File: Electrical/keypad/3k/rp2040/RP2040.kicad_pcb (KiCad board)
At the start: 4 copper layers, 67.7 x 67.4 mm, 79 parts, among them J1 Conn_01x04_Socket, P1 USB-TYPE-C-016, Q1 BSS138, SW1 TS-1187A-B-A-B, SW2 TS-1187A-B-A-B, SW3 BUTT1, SW4 BUTT3, SW5 BUTT2, U1 PRTR5V0U2X, U2 ME6208A44M3G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

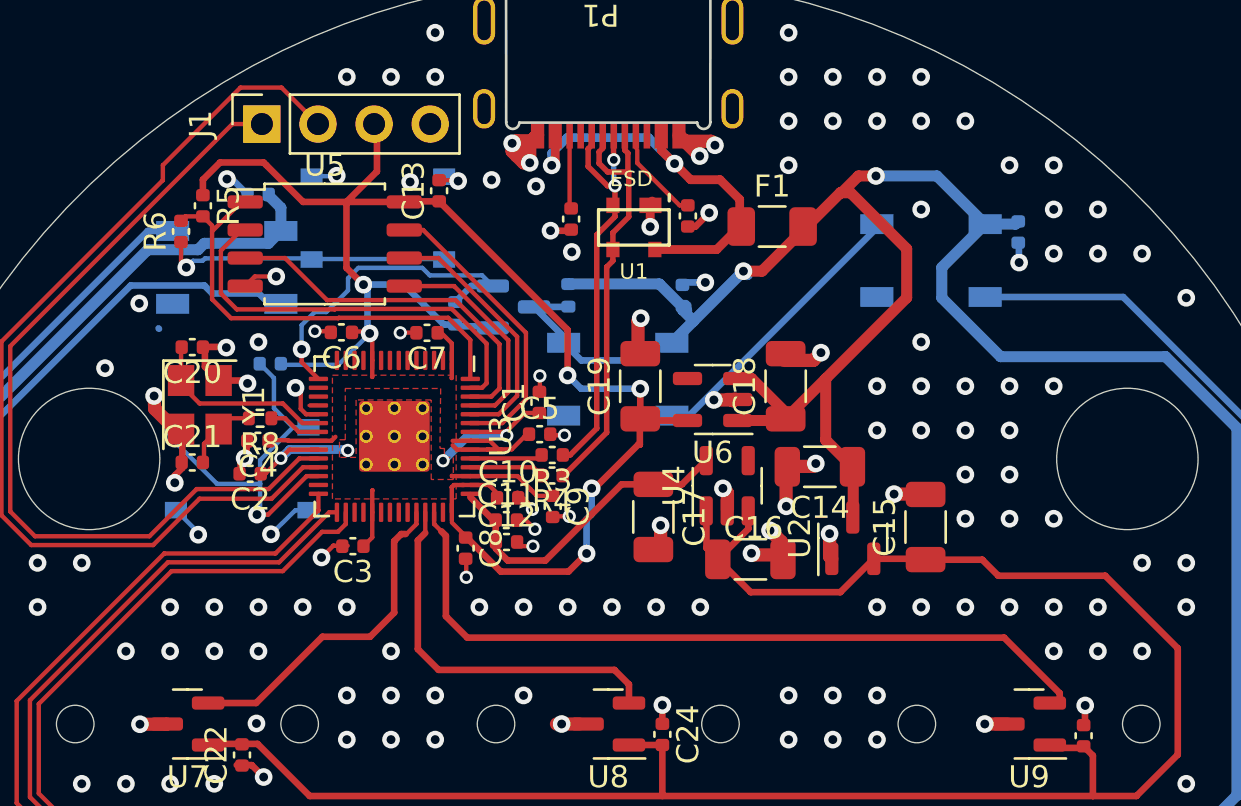
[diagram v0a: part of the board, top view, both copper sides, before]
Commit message: improves component placement
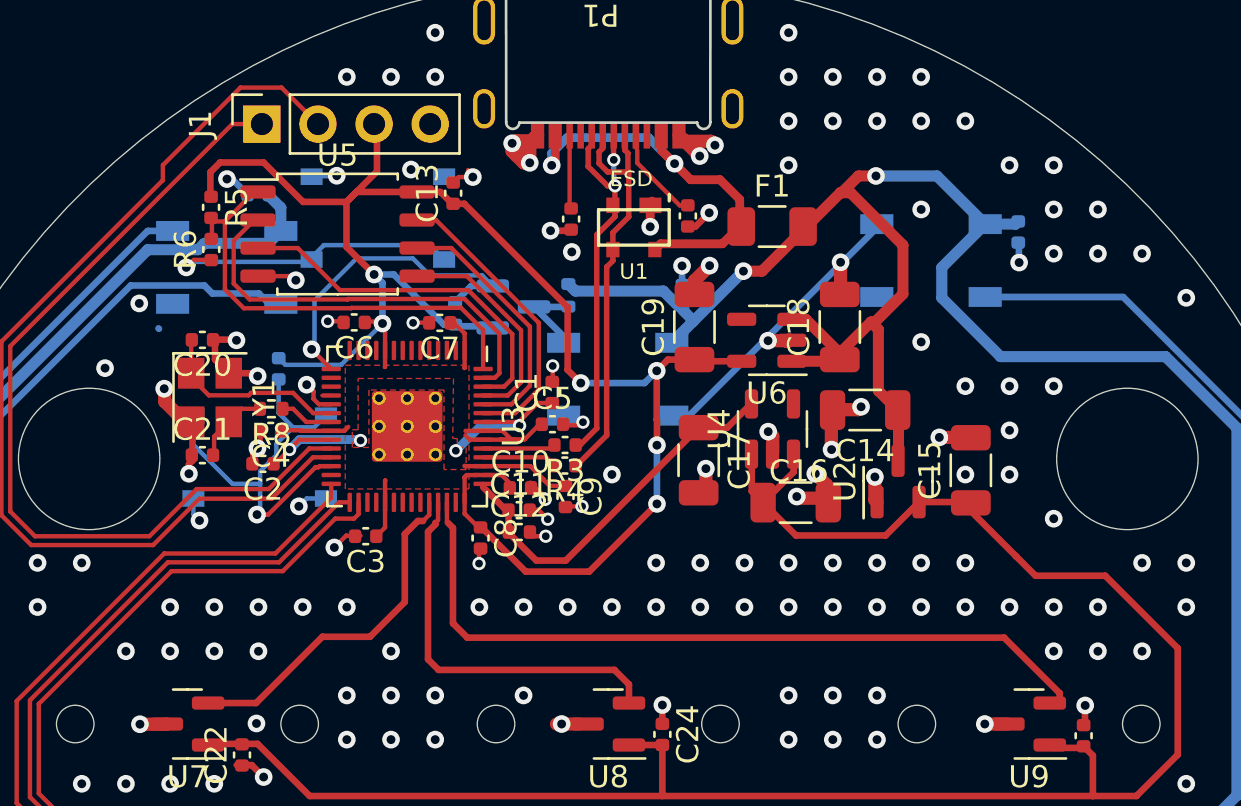
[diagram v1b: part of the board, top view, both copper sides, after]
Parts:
- moved U6 3.63 mm to (107.2, 82.6)
- moved C18 3.63 mm to (110.5, 82.0)
- moved C19 3.63 mm to (103.9, 82.0)
- moved C14 3.29 mm to (111.6, 85.8)
- moved U4 3.29 mm to (107.4, 86.6)
- moved C15 3.29 mm to (116.4, 88.5)
- moved C17 3.29 mm to (104.1, 88.1)
- moved U2 3.29 mm to (113.1, 89.0)
- moved C16 3.29 mm to (108.5, 90.0)
- moved R6 1.60 mm to (82.0, 78.5)
- moved SW2 0.95 mm to (84.2, 87.9)
- moved C8 0.82 mm to (94.2, 91.6)
- moved C10 0.73 mm to (96.0, 89.3)
- moved C12 0.73 mm to (96.0, 91.3)
- moved C3 0.73 mm to (89.0, 91.5)
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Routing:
- net +5V: track 273.7 -> 269.2 mm
- net Net-(D4-DIN): track 6.76 -> 3.41 mm
- net +3V3: track 88.1 -> 91.3 mm
- net ADC_AVDD: track 14.8 -> 17.4 mm
- net GND: track 93.8 -> 91.5 mm, vias 313 -> 315
- net +4V4: track 87.6 -> 86.7 mm
- net BUTT2: track 71.1 -> 71.9 mm
- net USB_D+: track 19.1 -> 18.4 mm
- net SWDIO: track 44.4 -> 45.2 mm
- net BUTT1: track 59.2 -> 59.9 mm
- net SWCLK: track 38.9 -> 39.7 mm
- net USB_D-: track 20.0 -> 19.3 mm
- net ADC_IN1: track 15.2 -> 15.8 mm
- net BUTT0: track 48.7 -> 49.4 mm
- net /QSPI_SS: track 21.3 -> 20.7 mm
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
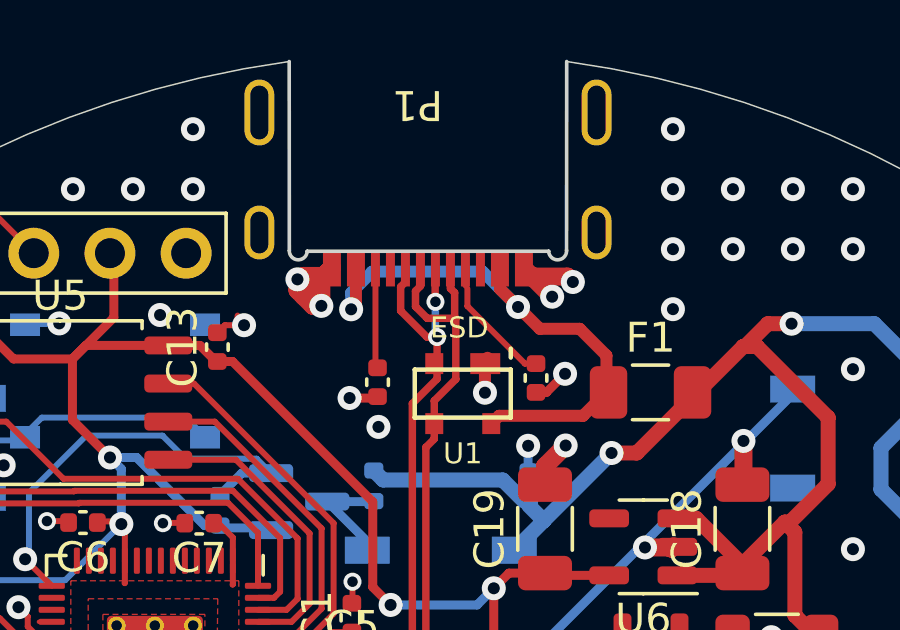
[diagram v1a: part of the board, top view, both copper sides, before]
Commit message: adds gnd vias near connector
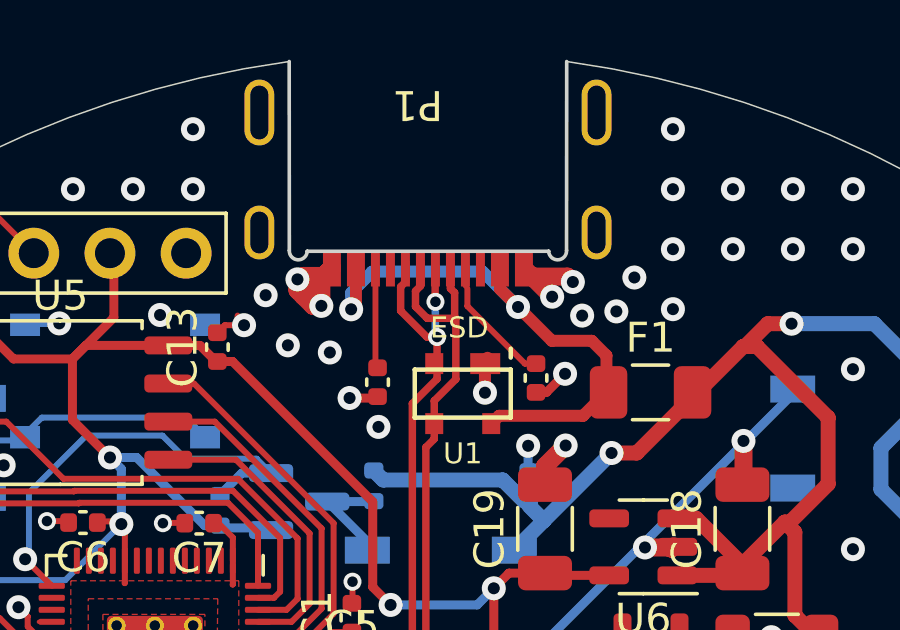
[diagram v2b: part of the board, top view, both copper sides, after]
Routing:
- net GND: vias 315 -> 321
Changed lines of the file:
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@@
   (via (at 104.166 130.706) (size 0.8) (drill 0.4) (layers "F.Cu" "B.Cu") (free) (net 1))
   (via (at 114.166 70.706) (size 0.8) (drill 0.4) (layers "F.Cu" "B.Cu") (free) (net 1))
+  (via (at 105.14 74.92) (size 0.8) (drill 0.4) (layers "F.Cu" "B.Cu") (free) (net 1))
   (via (at 112.166 128.706) (size 0.8) (drill 0.4) (layers "F.Cu" "B.Cu") (free) (net 1))
   (via (at 110.166 70.706) (size 0.8) (drill 0.4) (layers "F.Cu" "B.Cu") (free) (net 1))
@@
   (via (at 111.76 123.19) (size 0.8) (drill 0.4) (layers "F.Cu" "B.Cu") (free) (net 1))
   (via (at 100.166 88.706) (size 0.8) (drill 0.4) (layers "F.Cu" "B.Cu") (free) (net 1))
+  (via (at 94.59 74.24) (size 0.8) (drill 0.4) (layers "F.Cu" "B.Cu") (free) (net 1))
   (via (at 112.166 108.706) (size 0.8) (drill 0.4) (layers "F.Cu" "B.Cu") (free) (net 1))
   (via (at 93.135 123.165) (size 0.8) (drill 0.4) (layers "F.Cu" "B.Cu") (net 1))
@@
   (via (at 88.166 70.706) (size 0.8) (drill 0.4) (layers "F.Cu" "B.Cu") (free) (net 1))
   (via (at 114.166 128.706) (size 0.8) (drill 0.4) (layers "F.Cu" "B.Cu") (free) (net 1))
+  (via (at 95.33 75.91) (size 0.8) (drill 0.4) (layers "F.Cu" "B.Cu") (free) (net 1))
   (via (at 98.815162 90.1495) (size 0.6) (drill 0.35) (layers "F.Cu" "B.Cu") (net 1))
   (via (at 88.166 106.706) (size 0.8) (drill 0.4) (layers "F.Cu" "B.Cu") (free) (net 1))
@@
   (via (at 92.166 112.706) (size 0.8) (drill 0.4) (layers "F.Cu" "B.Cu") (free) (net 1))
   (via (at 108.166 130.706) (size 0.8) (drill 0.4) (layers "F.Cu" "B.Cu") (free) (net 1))
+  (via (at 106.28 74.78) (size 0.8) (drill 0.4) (layers "F.Cu" "B.Cu") (free) (net 1))
   (via (at 86.166 112.706) (size 0.8) (drill 0.4) (layers "F.Cu" "B.Cu") (free) (net 1))
   (via (at 130.166 98.706) (size 0.8) (drill 0.4) (layers "F.Cu" "B.Cu") (free) (net 1))
@@
   (via (at 108.166 112.706) (size 0.8) (drill 0.4) (layers "F.Cu" "B.Cu") (free) (net 1))
   (via (at 114.166 106.706) (size 0.8) (drill 0.4) (layers "F.Cu" "B.Cu") (free) (net 1))
+  (via (at 96.73 76.15) (size 0.8) (drill 0.4) (layers "F.Cu" "B.Cu") (free) (net 1))
   (via (at 96.166 94.706) (size 0.8) (drill 0.4) (layers "F.Cu" "B.Cu") (free) (net 1))
   (via (at 84.075 99.975) (size 0.8) (drill 0.4) (layers "F.Cu" "B.Cu") (free) (net 1))
@@
   (via (at 88.166 108.706) (size 0.8) (drill 0.4) (layers "F.Cu" "B.Cu") (free) (net 1))
   (via (at 74.166 94.706) (size 0.8) (drill 0.4) (layers "F.Cu" "B.Cu") (free) (net 1))
+  (via (at 106.88 73.65) (size 0.8) (drill 0.4) (layers "F.Cu" "B.Cu") (free) (net 1))
   (via (at 98.166 94.706) (size 0.8) (drill 0.4) (layers "F.Cu" "B.Cu") (free) (net 1))
   (via (at 108.166 124.706) (size 0.8) (drill 0.4) (layers "F.Cu" "B.Cu") (free) (net 1))
@@
   (segment (start 77.2 108.65) (end 77.01 108.67) (width 0.2) (layer "B.Cu") (net 1))
   (segment (start 104.045 107.145) (end 104.045 107.195) (width 0.3) (layer "B.Cu") (net 1))
-  (segment (start 105.06 75.36) (end 105.95 76.25) (width 0.4) (layer "F.Cu") (net 2))
   (segment (start 105.95 77.48) (end 105.17 78.26) (width 0.4) (layer "F.Cu") (net 2))
+  (segment (start 104.129891 75.76) (end 105.46 75.76) (width 0.4) (layer "F.Cu") (net 2))
+  (segment (start 105.46 75.76) (end 105.95 76.25) (width 0.4) (layer "F.Cu") (net 2))
+  (segment (start 103.002858 74.632967) (end 104.129891 75.76) (width 0.4) (layer "F.Cu") (net 2))
+  (segment (start 102.4 74.030109) (end 102.4 73.225) (width 0.4) (layer "F.Cu") (net 2))
   (segment (start 105.95 76.25) (end 105.95 77.48) (width 0.4) (layer "F.Cu") (net 2))
-  (segment (start 102.37 78.26) (end 102.11 78.52) (width 0.4) (layer "F.Cu") (net 2))
-  (segment (start 102.4 74.030109) (end 102.4 73.225) (width 0.4) (layer "F.Cu") (net 2))
-  (segment (start 103.729891 75.36) (end 105.06 75.36) (width 0.4) (layer "F.Cu") (net 2))
+  (segment (start 105.17 78.26) (end 102.37 78.26) (width 0.4) (layer "F.Cu") (net 2))
   (segment (start 103.002858 74.632967) (end 102.4 74.030109) (width 0.4) (layer "F.Cu") (net 2))
   (segment (start 97.6 74.55) (end 97.6 73.325) (width 0.4) (layer "F.Cu") (net 2))
-  (segment (start 105.17 78.26) (end 102.37 78.26) (width 0.4) (layer "F.Cu") (net 2))
-  (segment (start 103.002858 74.632967) (end 103.729891 75.36) (width 0.4) (layer "F.Cu") (net 2))
+  (segment (start 102.37 78.26) (end 102.11 78.52) (width 0.4) (layer "F.Cu") (net 2))
   (segment (start 97.44 74.71) (end 97.6 74.55) (width 0.4) (layer "F.Cu") (net 2))
   (via (at 103.002858 74.632967) (size 0.8) (drill 0.4) (layers "F.Cu" "B.Cu") (net 2))

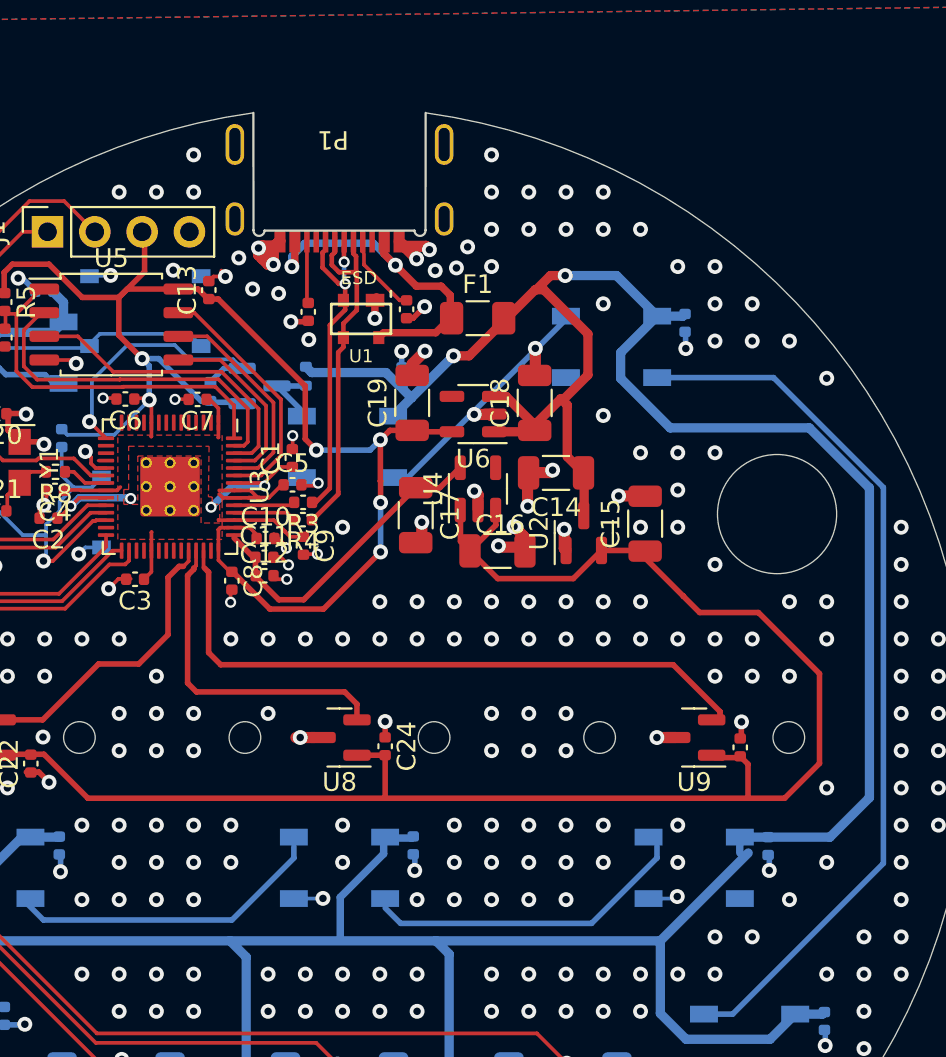
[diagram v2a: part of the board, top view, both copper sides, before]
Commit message: improves case and pcb
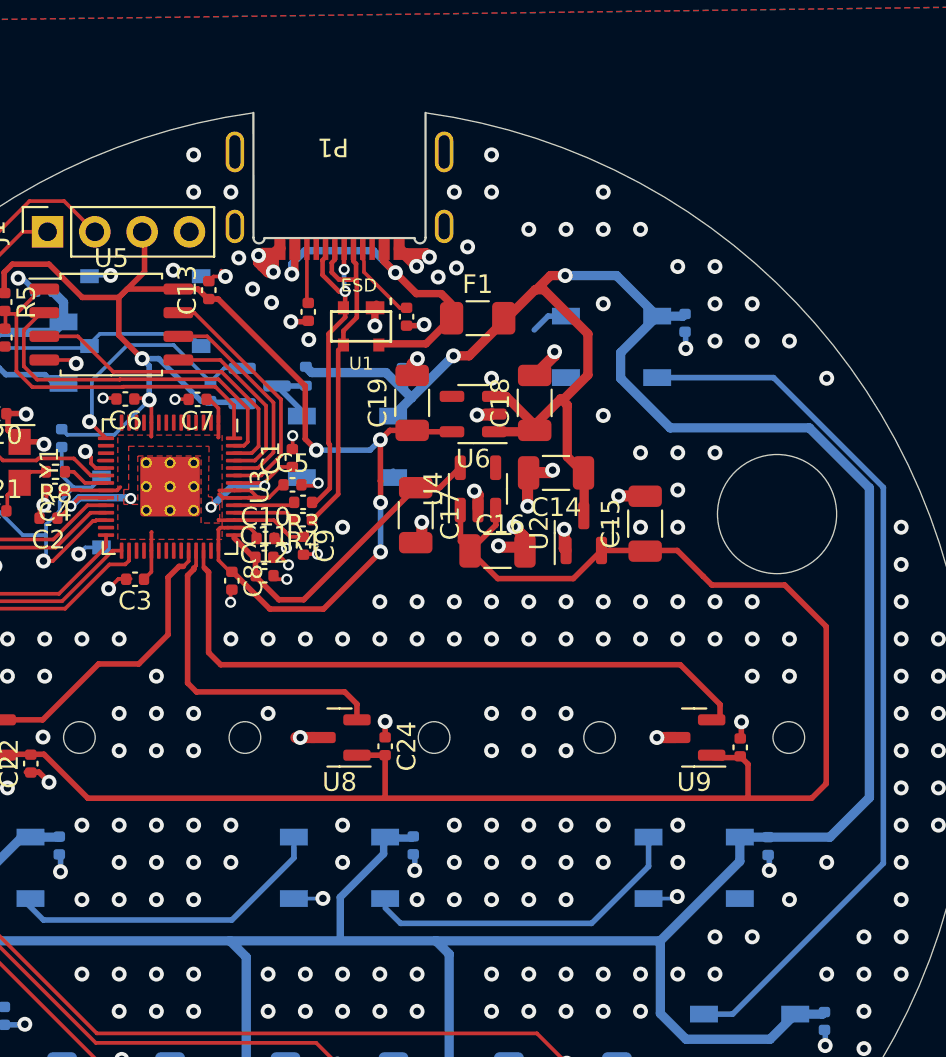
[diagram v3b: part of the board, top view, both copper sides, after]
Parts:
- moved R1 0.40 mm to (103.6, 77.4)
- moved U1 0.40 mm to (101.2, 77.9)
- moved P1 0.40 mm to (100.0, 68.5)
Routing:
- net Net-(D4-DOUT): track 13.0 -> 2.36 mm
- net +4V4: track 86.7 -> 89.5 mm
- net LED_D: track 14.9 -> 13.5 mm
- net +5V: track 269.2 -> 269.9 mm
- net GND: track 91.5 -> 91.0 mm, vias 321 -> 315
- net VBUS: track 19.3 -> 19.9 mm

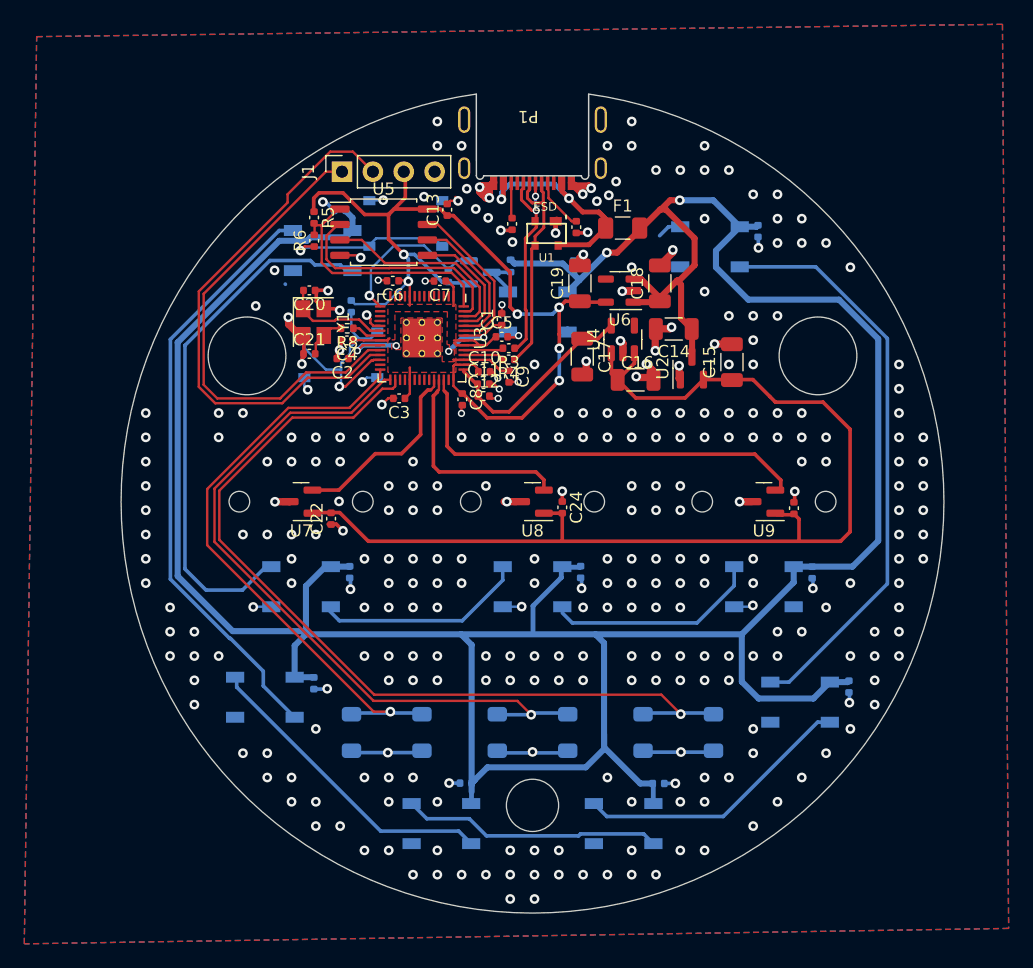
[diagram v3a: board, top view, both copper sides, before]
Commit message: creates outline with screw and 3d printed standoffs, and space for panelization mousebites to be put for better case fit.
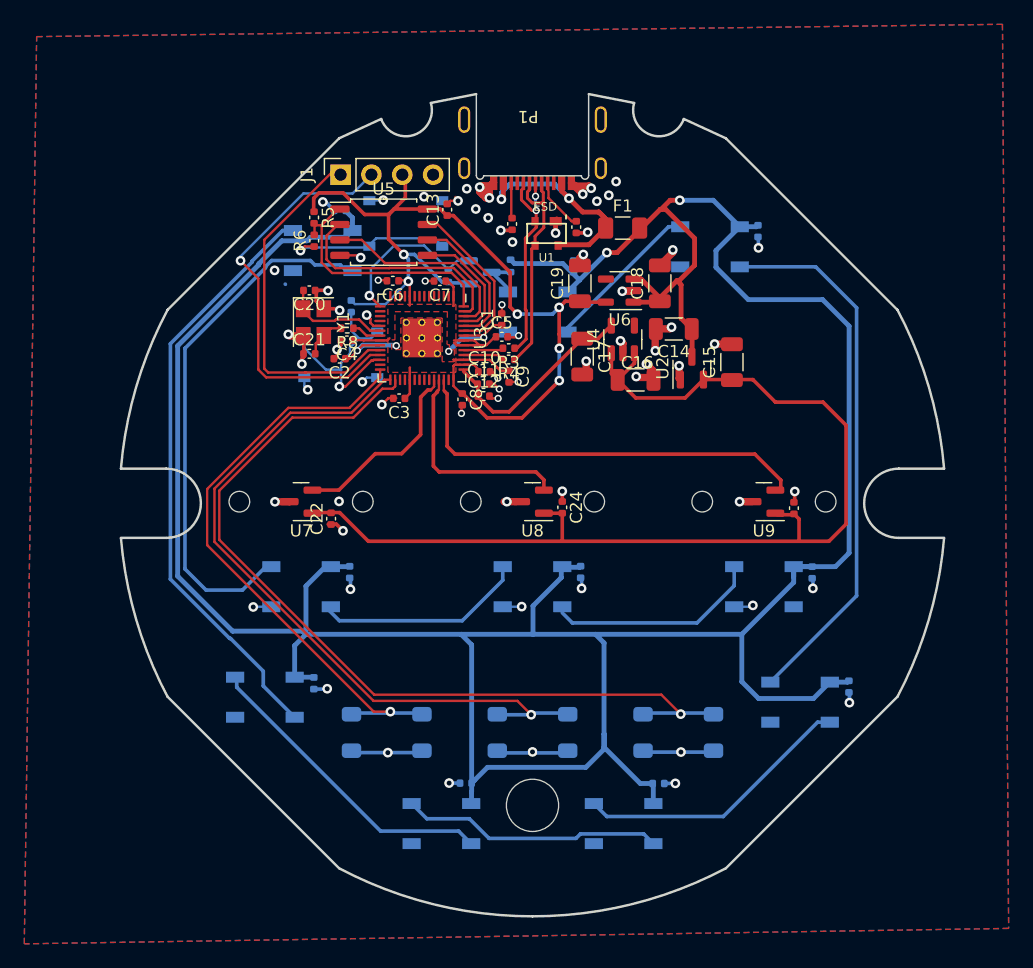
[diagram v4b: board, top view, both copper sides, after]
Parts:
- removed H1, H2: MountingHole_6.4mm_M6_DIN965, MountingHole:MountingHole_6.4mm_M6_DIN965
- removed H3: MountingHole_4.3mm_M4_DIN965, MountingHole:MountingHole_4.3mm_M4_DIN965
- added REF**: MountingHole_4.3mm_M4, MountingHole:MountingHole_4.3mm_M4, F.Cu at (100.0, 125.0)
- moved J1 0.27 mm to (84.2, 73.1)
- moved C2 0.25 mm to (84.1, 88.2)
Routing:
- net Net-(D4-DOUT): track 2.36 -> 13.1 mm
- net SWDIO: track 45.2 -> 34.5 mm, vias 0 -> 1
- net SWCLK: track 39.7 -> 29.8 mm
- net +5V: track 269.9 -> 266.1 mm
- net Net-(D5-DOUT): track 48.0 -> 45.0 mm
- net GND: track 91.0 -> 89.9 mm, vias 315 -> 70
- net +4V4: track 89.5 -> 88.7 mm
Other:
- board size 67.7 x 67.4 mm -> 67.8 x 67.7 mm
